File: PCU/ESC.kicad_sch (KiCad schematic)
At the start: 50 parts, among them IC1 TCAN3403DDFRQ1, IC2 UCC27211DR, IC3 UCC27211DR, IC4 UCC27211DR, J1 JST PH 4Pin, J2 JST SH 5Pin, J3 JST SH 3Pin

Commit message: ESC Block Updated
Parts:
- removed C10, C14, C9: 0.1uF 50V, Capacitor_SMD:C_0603_1608Metric, symbol Device:C
- removed C15, C16, C17, C2: 15nF, Capacitor_SMD:C_0603_1608Metric, symbol Device:C
- removed D3: SS0540_R1_00001, BassingaLib_Diodes:SOD3816X135N, symbol BassingaLib_Diodes:SS0540_R1_00001
- removed J1: JST PH 4Pin, BassinaLib_Connectors:S4B-PH-SM4-TB, symbol BassinaLib_Connectors:S4B-PH-SM4-TB_LF__SN_
- removed R1, R2: 33k 1%, Resistor_SMD:R_0603_1608Metric, symbol Device:R
- removed R18, R19, R20: 680R 1%, Resistor_SMD:R_0603_1608Metric, symbol Device:R
- removed R3: 120R 1%, Resistor_SMD:R_0603_1608Metric, symbol Device:R
- removed R6: 68k 1%, Resistor_SMD:R_0603_1608Metric, symbol Device:R
- removed R7: 10k 1%, Resistor_SMD:R_0603_1608Metric, symbol Device:R
- removed R8: 180k 1%, Resistor_SMD:R_0603_1608Metric, symbol Device:R
- removed S1: SPST Switch, BassinaLib_Switch:DS04254201BKSMT, symbol BassinaLib_Switch:DS04-254-2-01BK-SMT
- added C12: 15nF, Capacitor_SMD:C_0603_1608Metric, symbol Device:C
- added C3: 1nF, Capacitor_SMD:C_0603_1608Metric, symbol Device:C
- added D1, D5: SS0540_R1_00001, BassingaLib_Diodes:SOD3816X135N, symbol BassingaLib_Diodes:SS0540_R1_00001
- added R12, R4: 51R 1%, Resistor_SMD:R_0603_1608Metric, symbol Device:R
- C1, C5: value 15nF -> 1nF; Manufacturer_Name Samsung Electro-Mechanics -> KYOCERA AVX; Manufacturer_Part_Number CL10B153KB8NNNC -> KAF15AR71H102KM
- R9: value 18k 1% -> 51R 1%; Manufacturer_Part_Number AC0603FR-1318KL -> RT0603FRE0751RL
- renumbered C12 to C10, C13 to C11, C3 to C2, C11 to C9, D1 to D2, D2 to D3, J2 to J7, J3 to J8, R14 to R10, R15 to R11, R16 to R13, R17 to R14, R10 to R2, R12 to R3, R4 to R5, R5 to R6, R11 to R7, R13 to R8
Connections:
- net V3.3_Mesure is gone; now on net Phase_1: C1.2
- net GND: now also C12.1, C3.1; no longer R9.1
- net Phase_1: now also R4.2; no longer R2.2, R3.2
- net Phase_2: now also R9.2, C3.2; no longer R7.2, R8.2
- net Phase_3: now also C5.2, R12.2; no longer R10.2, R11.2
- net +12V renamed +12V_PWR
- net +3.3V renamed +3.3V_PWR
- net +3.3V_PWR: now also D1.1 (K), D5.1 (K)
- net CANH renamed ESC_CANH
- net CANL renamed ESC_CANL
- net MCU/FDCAN2_RX renamed MCU/FDCAN1_RX
- net MCU/FDCAN2_STB renamed MCU/FDCAN1_STB
- net MCU/FDCAN2_TX renamed MCU/FDCAN1_TX
- net MCU/UART2_RX renamed MCU/UART1_RX
- net MCU/UART1_RX: now also D2.1; no longer D2.2
- net MCU/UART2_TX renamed MCU/UART1_TX
- net MCU/UART1_TX: now also D2.2; no longer D2.1
- net PCB_Temp renamed ESC_Temp
- net ESC_Temp: now also C12.2
- removed net Vbus_Mesure: C5.2, D4.2 (A), R9.2
- new net: D1.2 (A), R2.2, R3.2, R4.1
- new net: D5.2 (A), R10.2, R11.2, R12.1
- new net: D4.2 (A), R7.2, R8.2, R9.1
- no-connect marks 1 -> 0
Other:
- sheet Half-Bridge_1 ports: added none; removed Vshunt_B
- sheet Half-Bridge_2 ports: added none; removed Vshunt_B
- sheet Half-Bridge_3 ports: added none; removed Vshunt_B
- sheet MCU ports: added ESC_Temp, FDCAN1_RX, FDCAN1_STB, FDCAN1_TX, UART1_RX, UART1_TX; removed FDCAN2_RX, FDCAN2_STB, FDCAN2_TX, PCB_Temp, PWM_BREAK, UART2_RX, UART2_TX, V12_Mesure, V3.3_Mesure, Vbus_Mesure, Vshunt_1, Vshunt_2, Vshunt_3
- note added: "ESC Temperature Mesurement"
- note added: "Programming Interface"
- note added: "UART Connector"
- note removed: "+12V Mesurement"
- note removed: "+3.3V Mesurement"
- note removed: "PCB Temperature Mesurement"
- note removed: "Voltage Bus Mesurement"
- moved on the sheet: C10, C11, C2, C4, C6, C7, C8, C9, D2, D3, IC1, IC2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

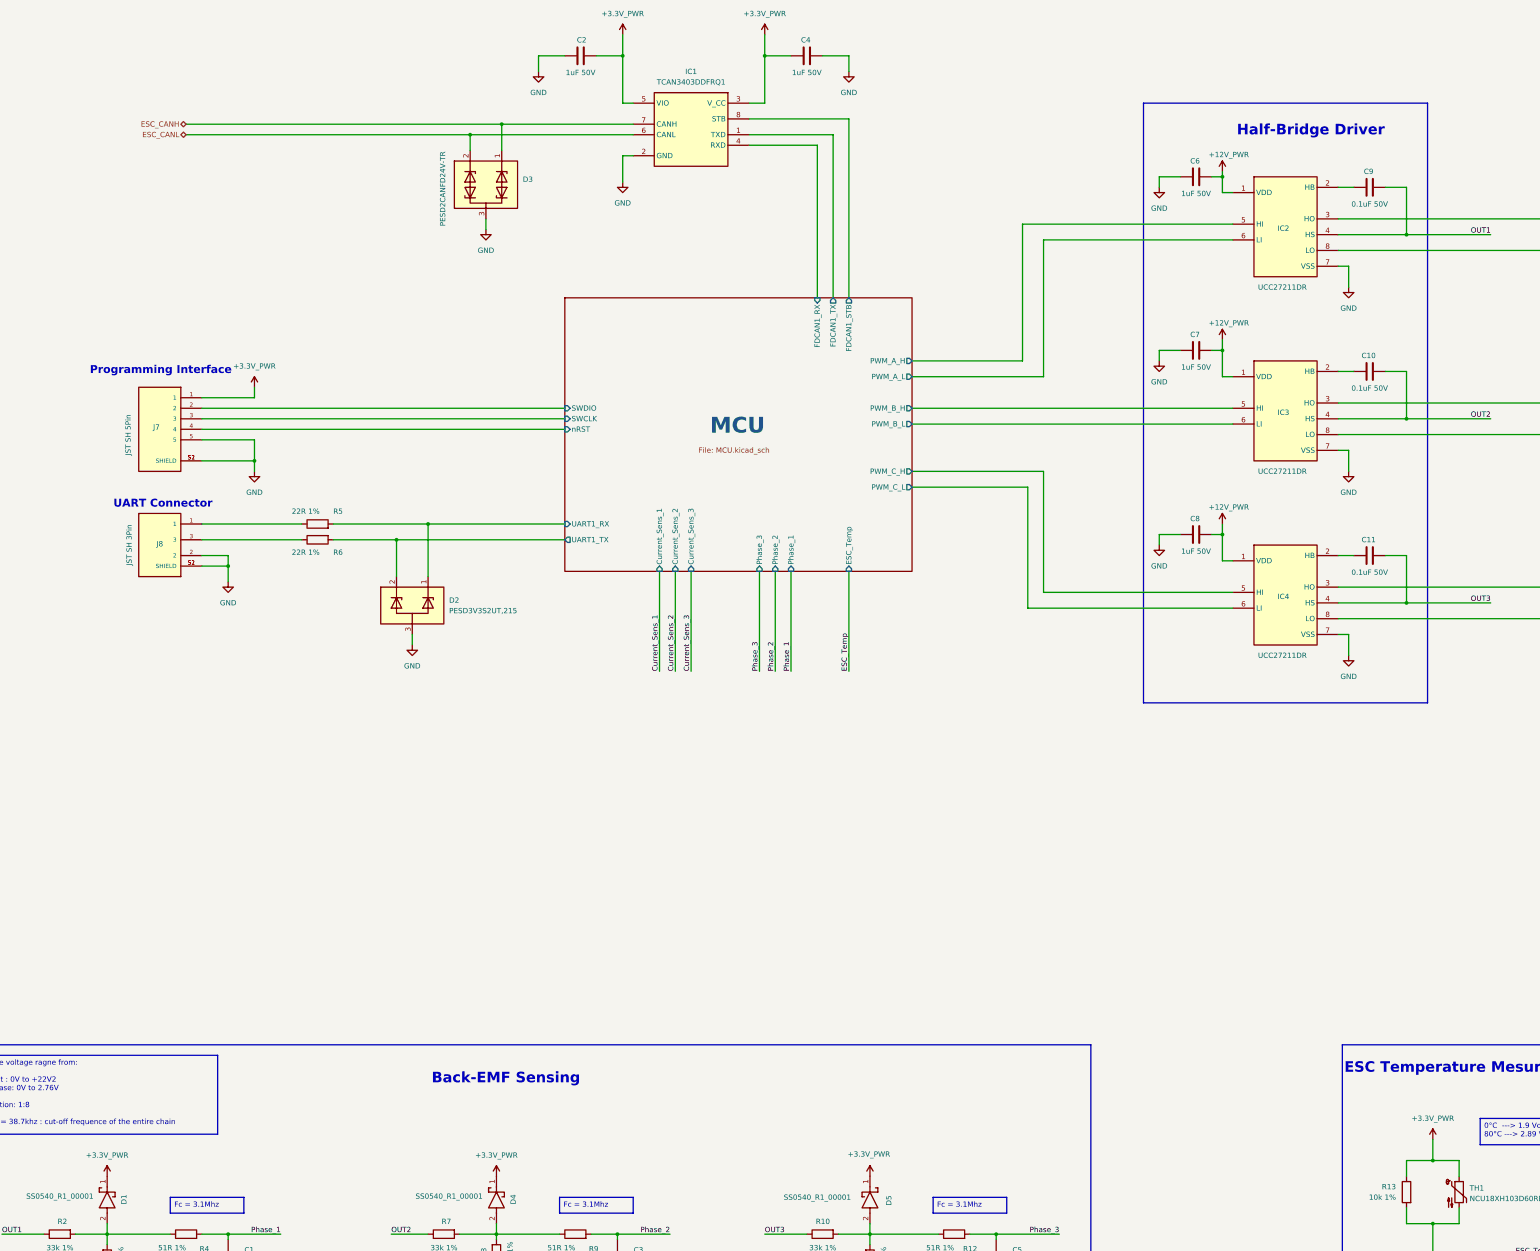
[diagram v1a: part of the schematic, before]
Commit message: high power supply block
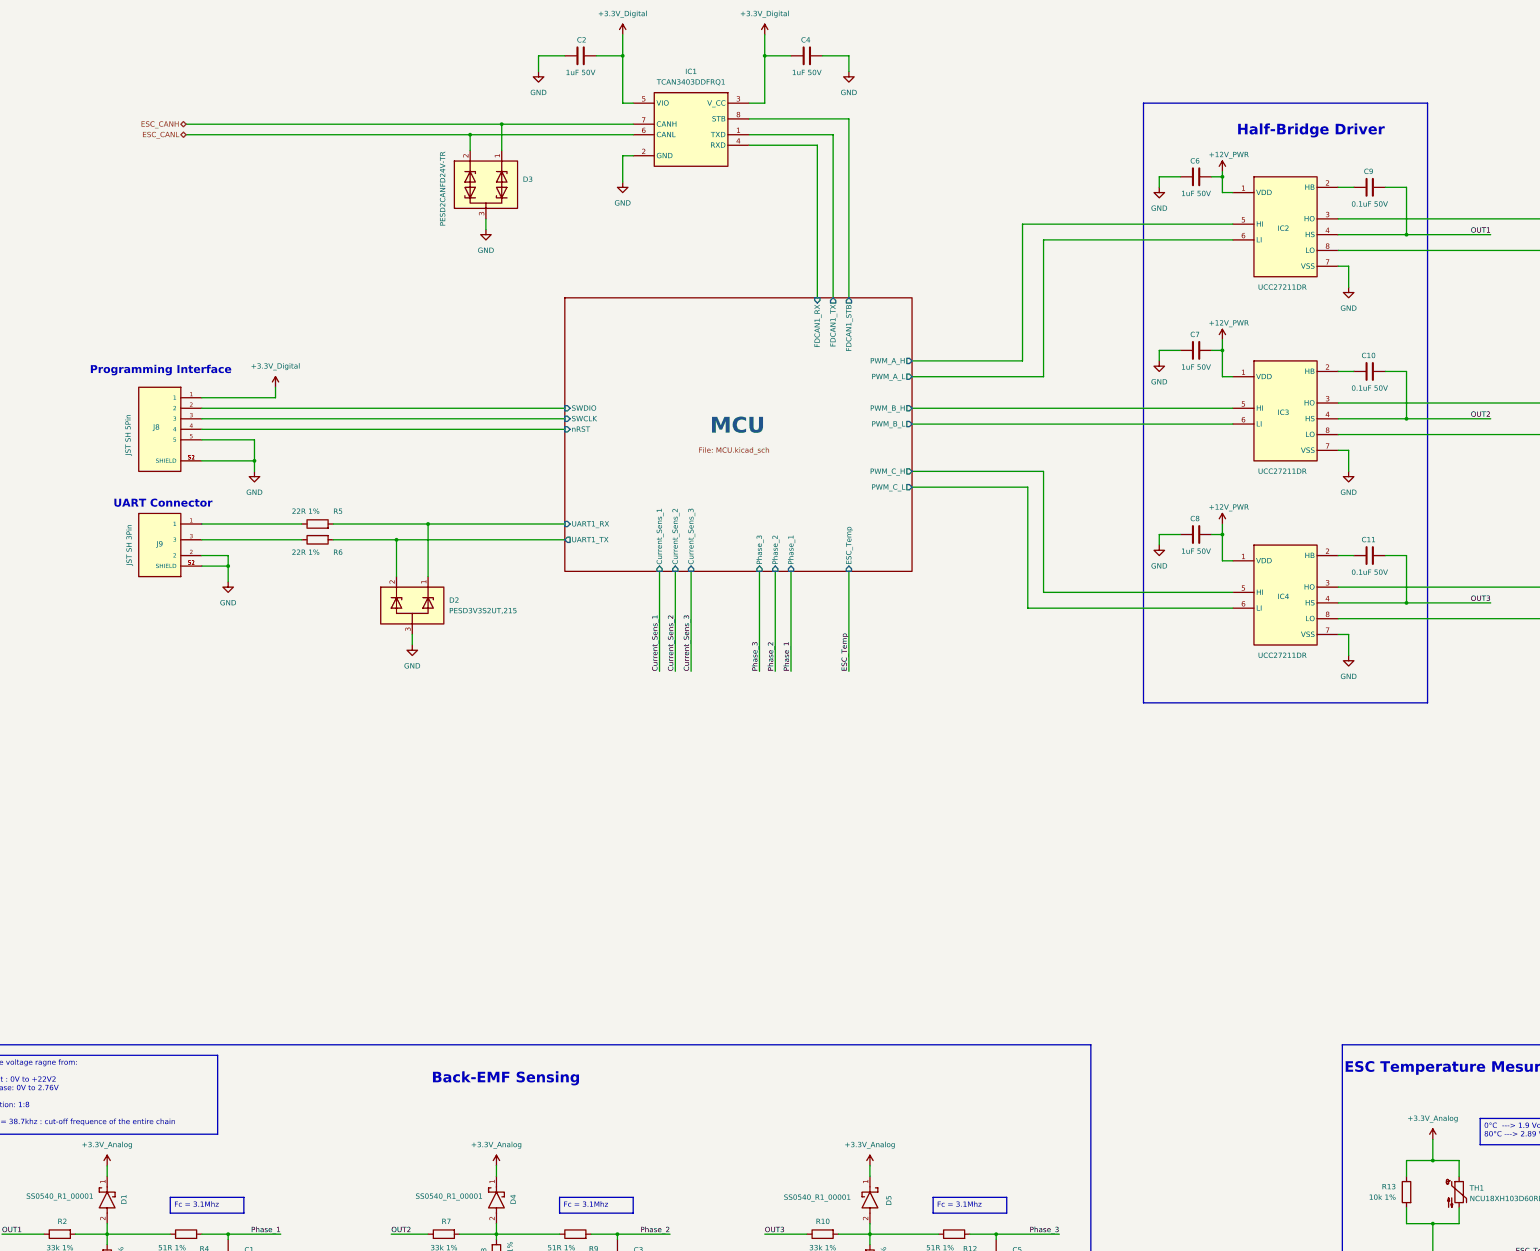
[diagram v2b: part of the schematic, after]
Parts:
- renumbered J7 to J8, J8 to J9
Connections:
- net +3.3V_PWR renamed +3.3V_Analog
- net +3.3V_Analog: no longer C2.1, C4.1, IC1.3 (V_CC), IC1.5 (VIO), J8.1
- new net +3.3V_Digital: C2.1, C4.1, IC1.3 (V_CC), IC1.5 (VIO), J8.1

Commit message: Supervisor Block
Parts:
- removed D3: PESD2CANFD24V-TR, BassingaLib_TVS:SOT95P230X110-3N, symbol BassingaLib_TVS:PESD2CANFD24V-TR
- renumbered D1 to D4, D2 to D5, D4 to D6, D5 to D7
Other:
- note added: "FD-CAN Interface"
- note added: "Programming Interface (SWD)"
- note added: "UART Interface"
- note removed: "Programming Interface"
- note removed: "UART Connector"

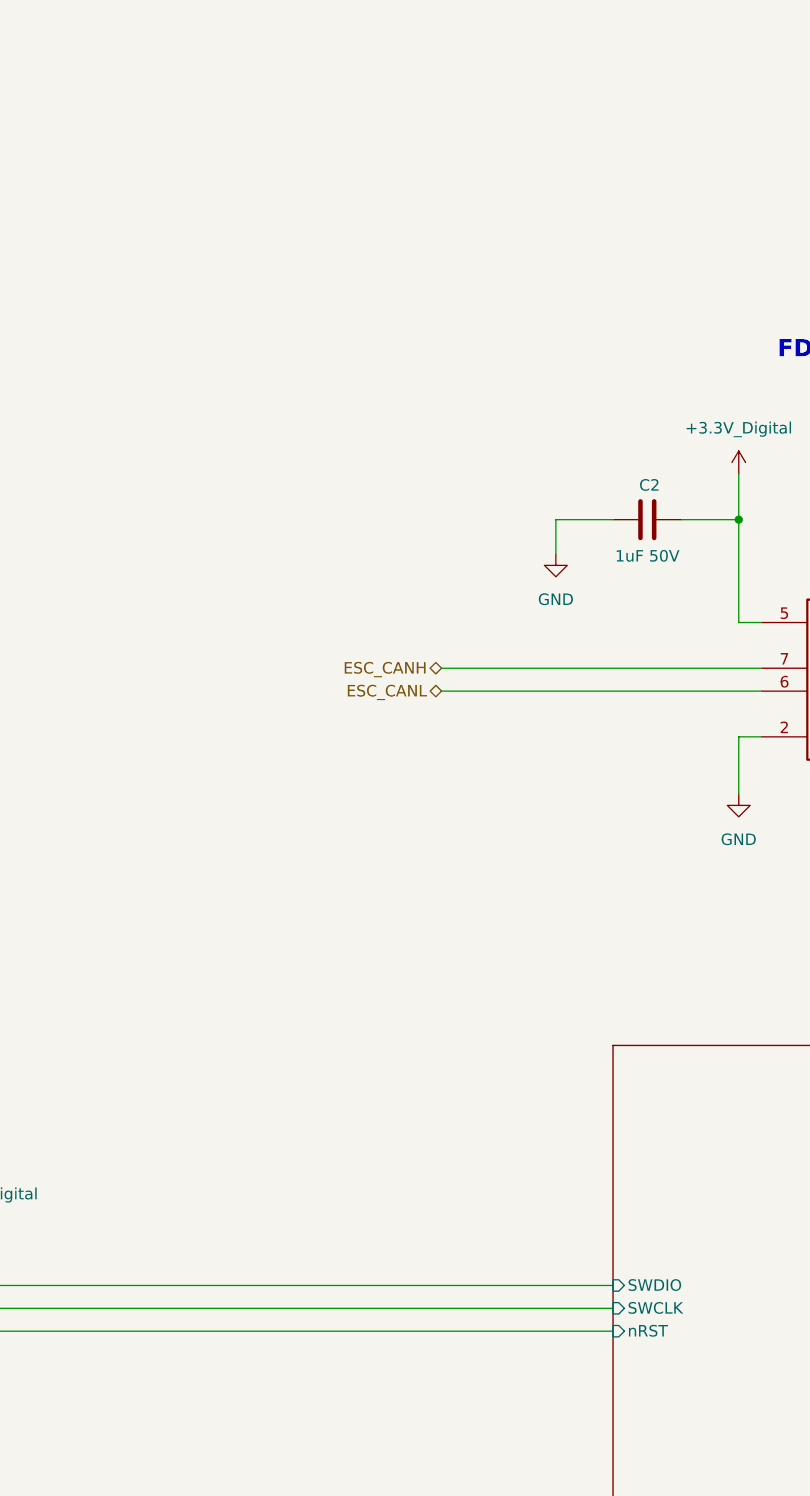
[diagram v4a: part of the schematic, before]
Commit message: ESCs Analog signals routed
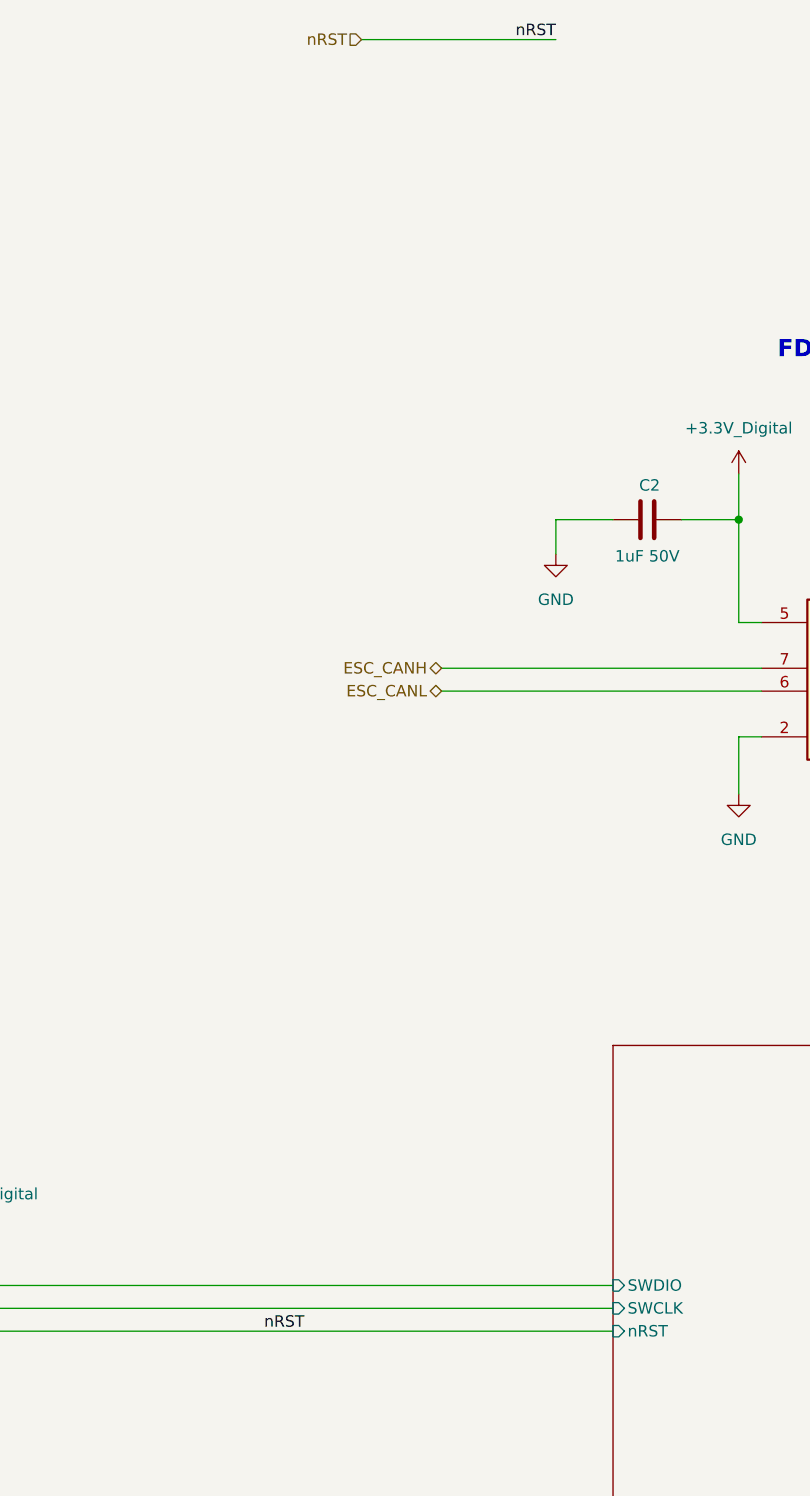
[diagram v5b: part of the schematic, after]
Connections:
- net MCU/nRST renamed nRST
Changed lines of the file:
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@@
+	(wire
+		(pts
+			(xy 147.32 33.02) (xy 168.91 33.02)
+		)
+		(stroke
+			(width 0)
+			(type default)
+		)
+	)
 	(wire
 		(pts
@@
 		)
 	)
+	(label "nRST"
+		(at 168.91 33.02 180)
+		(effects
+			(font
+				(size 1.27 1.27)
+			)
+			(justify right bottom)
+		)
+	)
 	(label "ESC_Temp"
 		(at 414.02 375.92 180)
@@
 			)
 			(justify left bottom)
+		)
+	)
+	(label "nRST"
+		(at 140.97 176.53 180)
+		(effects
+			(font
+				(size 1.27 1.27)
+			)
+			(justify right bottom)
 		)
 	)
@@
 		(effects
 			(font
+				(size 1.27 1.27)
+			)
+			(justify right)
+		)
+	)
+	(hierarchical_label "nRST"
+		(shape input)
+		(at 147.32 33.02 180)
+		(effects
+			(font

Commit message: Components library added
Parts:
- J8, J9: now in the parts list
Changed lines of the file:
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@@
 			)
 		)
-		(property "Datasheet" "~"
+		(property "Datasheet" "https://www.mouser.fr/datasheet/2/281/NCU18XH103D60RB-1519634.pdf"
 			(at 391.16 359.41 0)
 			(effects
@@
 		(unit 1)
 		(exclude_from_sim no)
-		(in_bom no)
+		(in_bom yes)
 		(on_board yes)
 		(dnp no)
@@
 		(unit 1)
 		(exclude_from_sim no)
-		(in_bom no)
+		(in_bom yes)
 		(on_board yes)
 		(dnp no)

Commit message: Fly controller design started
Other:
- company: BASSINGA Lab -> BASSINGA_LAB
- title: NovaDrone -> Propulsion Control Unit
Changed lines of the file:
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@@
 	(paper "A2")
 	(title_block
-		(title "NovaDrone")
+		(title "Propulsion Control Unit")
 		(date "2025-05-21")
 		(rev "v1.0")
-		(company "BASSINGA Lab")
+		(company "BASSINGA_LAB")
+		(comment 1 "Copyright © 2025 Andresse Brisel BASSINGA ")
 	)
 	(rectangle
